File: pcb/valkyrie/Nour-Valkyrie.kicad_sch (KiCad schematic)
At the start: 0 parts

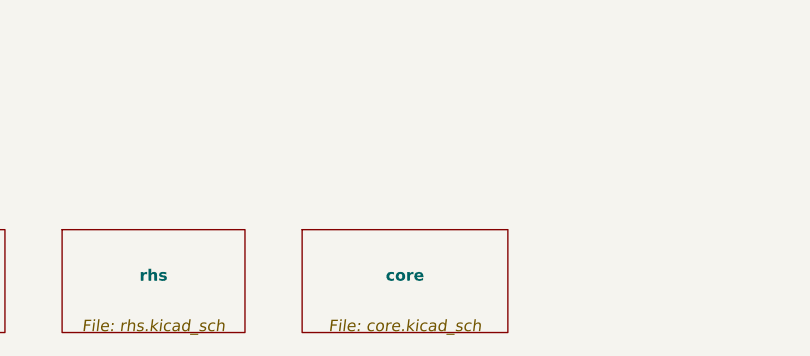
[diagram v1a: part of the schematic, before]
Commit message: Split the Core into a separate project
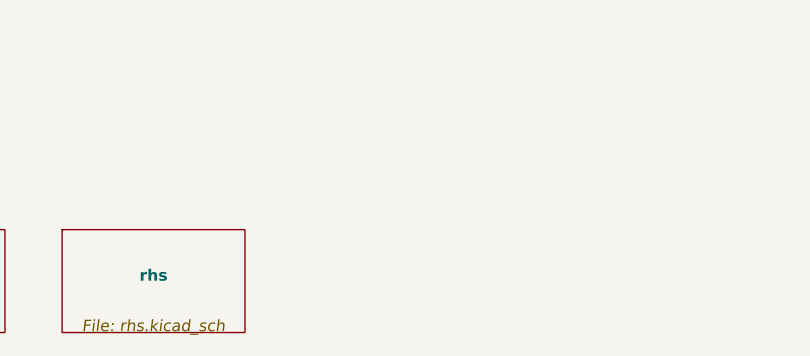
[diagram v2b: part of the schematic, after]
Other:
- removed sheet core
